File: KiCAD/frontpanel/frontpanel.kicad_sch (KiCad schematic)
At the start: 0 parts

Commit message: Drop empty stubs (PA/Driver/Balun/LPF_output/Front_Panel) from analog
None of these contributed components, nets, or PCB footprints on Rev A;
they were placeholder sub-sheets for future work. PA/Driver/Balun/
LPF_output will come back when the RF-chain board project is created
(a separate KiCAD/rf/ project, not part of analog). Front_Panel notes
were preserved by copying the text block into KiCAD/frontpanel/
frontpanel.kicad_sch first — the new frontpanel project is the actual
front-panel PCB.

Removed from analog.kicad_sch: five (sheet ...) blocks.
Removed from analog.kicad_pro: five UUID entries in the "sheets" list.
Deleted files: driver/pa/balun/lpf_output/front_panel.kicad_sch.

Rev A gerbers unaffected (fabricated 2026-07-14, byte-identical copy
preserved at KiCAD/analog/gerber/).

Co-Authored-By: Claude Opus 4.7 <noreply@anthropic.com>
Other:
- note added: "Front-panel vector board. Off-PCB. Connects to the main board's RJ45 J1 (on the Interface sheet) through a shielded CAT6 umbilical (T568B). See Documentation/front_panel_interface.md for wiring, grounding rules, and the open-items checklist. Parts to add here (all mark exclude_from_board = yes so KiCad does not try to route them on the main PCB): - Adafruit PCF8575 I2C 16-GPIO expander (I2C addr 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"
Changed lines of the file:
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@@
 	(generator_version "10.0")
 	(paper "A4")
+	(text "Front-panel vector board.\n\nOff-PCB. Connects to the main board's RJ45 J1 (on the Interface sheet)\nthrough a shielded CAT6 umbilical (T568B). See\nDocumentation/front_panel_interface.md for wiring, grounding rules,\nand the open-items checklist.\n\nParts to add here (all mark exclude_from_board = yes so KiCad\ndoes not try to route them on the main PCB):\n  - Adafruit PCF8575 I2C 16-GPIO expander (I2C addr 0x20)\n  - Winstar WH2004A 20x4 character LCD (driven in 4-bit mode by the PCF8575)\n  - 2x Bourns PEC11-4 mechanical encoders (STEP, FUNC)\n  - MBL-600 optical encoder (RS-422 differential, wired straight to the RJ45)\n  - Paddle jack (dit / dah -> PCF8575 GPIO)\n  - Front-panel LEDs (TX, fault, VFO-lock -> PCF8575 GPIO)\n  - Bypass caps at LCD Vcc and PCF8575 Vcc (10 uF + 100 nF each)\n  - LCD contrast trim pot, backlight series resistor"
+		(exclude_from_sim no)
+		(at 25.4 25.4 0)
+		(effects
+			(font
+				(size 1.27 1.27)
+			)
+			(justify left top)
+		)
+	)
 	(sheet_instances
 		(path "/"

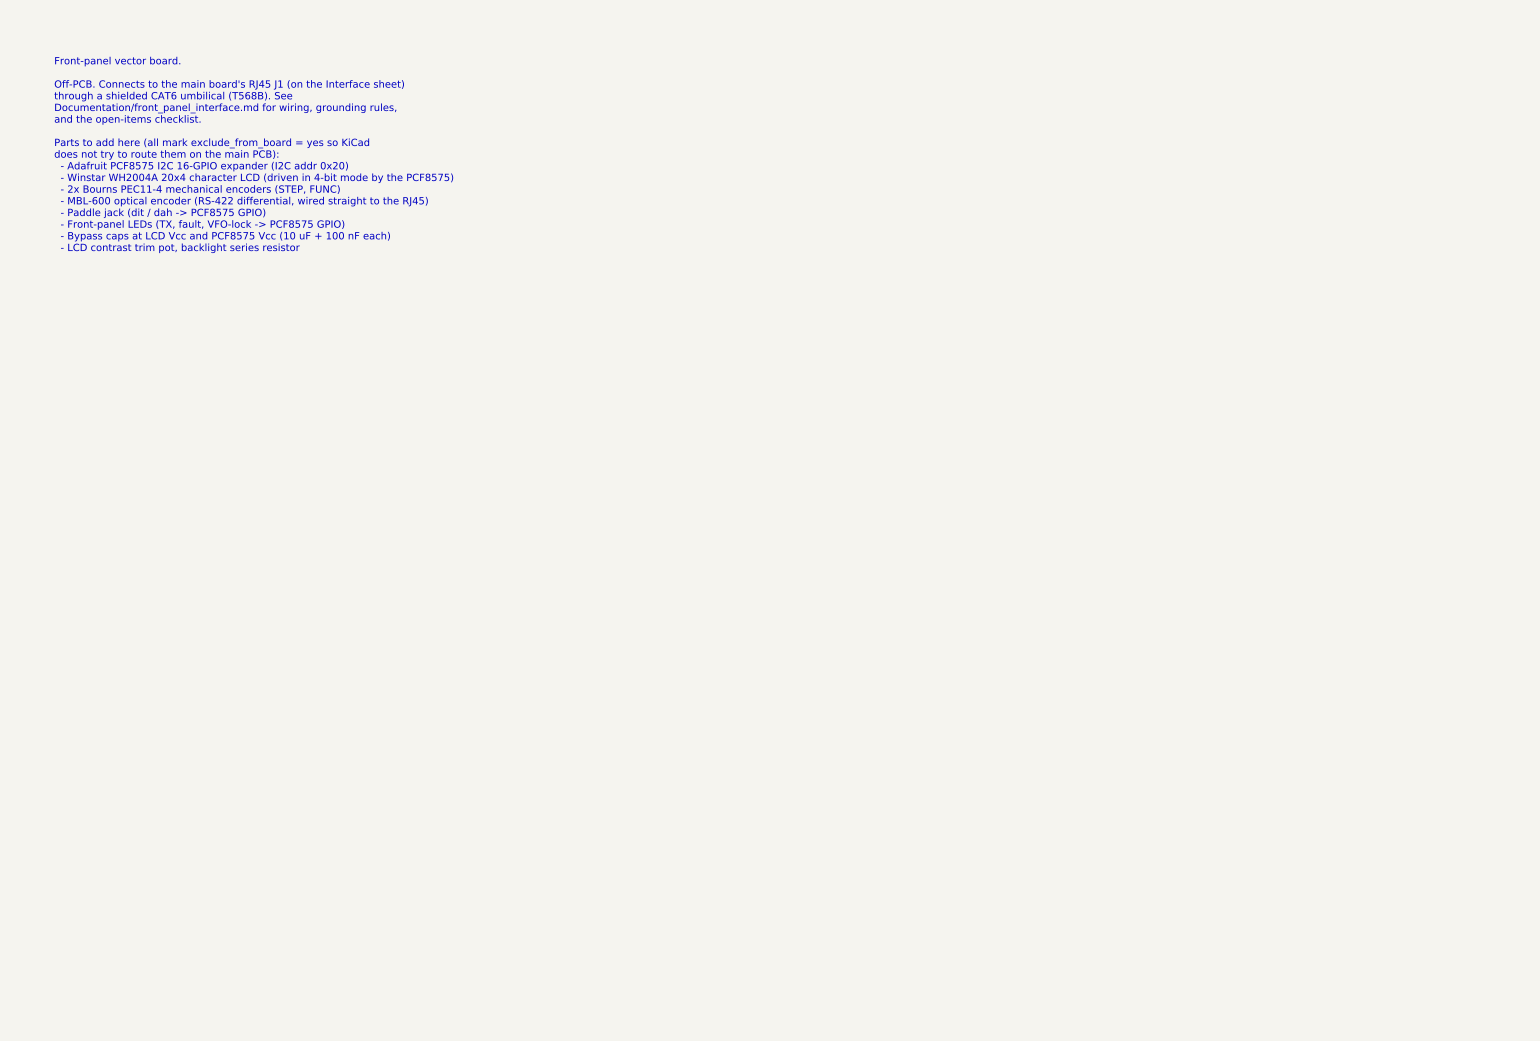
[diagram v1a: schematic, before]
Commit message: Front-panel PCB topology + I2C address plan alignment + 5734 symbol fix
Switch the front panel from a hand-wired vector board with a cut CAT6
pigtail to a real PCB with an Amphenol RJE1D-188-21401 socket at each
end of a commercial CAT6 patch cable. Shield ground stays single-point
at the analog board; the front-panel socket's shield-tab pads are left
floating on the schematic, with a GND-isolated PCB zone poured around
the connector body at layout time.

Reflect the current I2C address plan (updated 2026-07-15):
  - MCP4728  0x67  (was 0x62 in older docs -- reserves 0x62/0x63 for
                    future MCP4725 bias DACs)
  - STEP QT  0x37  (A0 jumper -- dodges the Metro's on-board MAX17048)
  - FUNC QT  0x38  (A1 jumper)
  - MAX17048 0x36  (documented as on the shared bus, not a private one)

Fix xmitter:Encoder_5734 (MBL600-100P-5L / Adafruit #5734) -- was a
3-pin single-ended stub, now the correct 6-pin RS-422 line-driver
symbol matching the actual datasheet (terminals 1=A, 2=B, 3=0V, 4=Vcc,
5=A-, 6=B-). Matches the AM26LS32 receiver on the analog interface sheet.

Add an optional second paddle path via the front-panel PCF8575 GPIO for
mechanical-build flexibility. Only one paddle path populated per build.

Reopen the RJE1D-188 footprint verification -- current footprint is
known wrong pending Rev A dry-fit; hold off on edits until Rev A arrives.

Sweeps stale post-reorg `KiCAD/interface.kicad_sch` paths to
`KiCAD/analog/interface.kicad_sch`.

Co-Authored-By: Claude Opus 4.7 <noreply@anthropic.com>
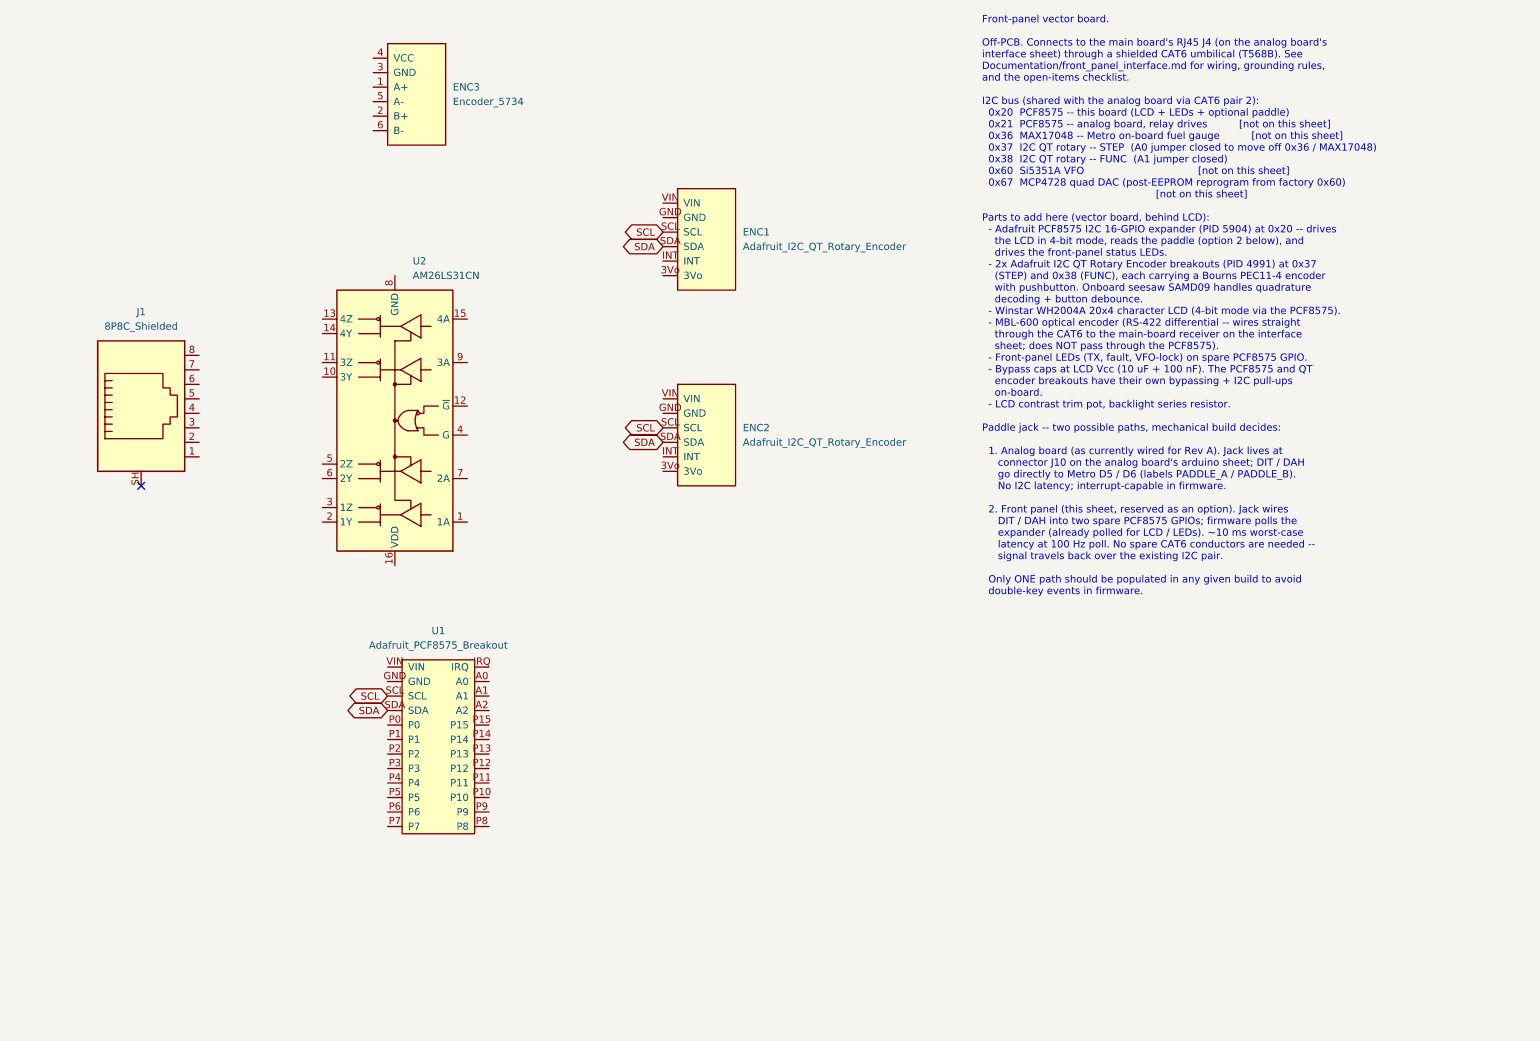
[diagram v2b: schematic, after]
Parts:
- added ENC1, ENC2: Adafruit_I2C_QT_Rotary_Encoder, xmitter:Adafruit_I2C_QT_Rotary_Encoder, symbol xmitter:Adafruit_I2C_QT_Rotary_Encoder
- added ENC3: Encoder_5734, Connector_PinHeader_2.54mm:PinHeader_1x06_P2.54mm_Vertical, symbol xmitter:Encoder_5734
- added J1: 8P8C_Shielded, xmitter:Amphenol_RJE1D-188_Horizontal_Shielded, symbol Connector:8P8C_Shielded
- added U1: Adafruit_PCF8575_Breakout, xmitter:Adafruit_PCF8575_Breakout, symbol xmitter:Adafruit_PCF8575_Breakout
- added U2: AM26LS31CN, Package_DIP:DIP-16_W7.62mm, symbol Interface:AM26LS31CN
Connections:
- new net SCL: ENC1.SCL, ENC2.SCL, U1.SCL
- new net SDA: ENC1.SDA, ENC2.SDA, U1.SDA
- no-connect marks 0 -> 1
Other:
- note added: "Front-panel vector board. Off-PCB. Connects to the main board's RJ45 J4 (on the analog board's interface sheet) through a shielded CAT6 umbilical (T568B). See Documentation/front_panel_interface.md for wiring, grounding rules, and the open-items checklist. I2C bus (shared with the analog board via CAT6 pair 2): 0x20 PCF8575 -- this board (LCD + LEDs + optional paddle) 0x21 PCF8575 -- analog board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"
- note removed: "Front-panel vector board. Off-PCB. Connects to the main board's RJ45 J1 (on the Interface sheet) through a shielded CAT6 umbilical (T568B). See Documentation/front_panel_interface.md for wiring, grounding rules, and the open-items checklist. Parts to add here (all mark exclude_from_board = yes so KiCad does not try to route them on the main PCB): - Adafruit PCF8575 I2C 16-GPIO expander (I2C addr 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"

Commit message: Front-panel schematic: complete wiring, MBL-600 pinout aligned with analog
Complete the front-panel schematic build-out. Initial MBL-600 <-> RJ45
wiring disagreed with the analog interface sheet's T568B pinout; rewired
to conform. ERC now passes with zero errors/warnings.

  - J1 (RJE1D-188): signal pins labeled per T568B, shield tabs NC
    (single-point ground stays at the analog board end).
  - ENC3 (MBL-600 / Adafruit #5734): A+/A-/B+/B- to RJ45 pins 3/6/7/8
    matching interface.kicad_sch J4.
  - LCD1 (WH2004A) 4-bit mode: DB4-DB7 to PCF8575 via LCD_D4..LCD_D7,
    DB0-DB3 marked NC, R/W tied to GND, RV1=10k contrast pot on V0.
  - Backlight: pin 15 to +5V direct; cathodes through R1/R2/R3
    (200/120/120R for lifetime-derated 15 mA per channel) into
    Q1/Q2/Q3 2N7000 low-side switches gated from PCF8575.

Add LCD_WH2004A symbol to xmitter.kicad_sym.

Also add datasheets for parts used: WH2004A LCD, Si5351-B (VFO),
AM26LS31 (MBL-600 line driver), scaa137 (Si5351 app note).

Co-Authored-By: Claude Opus 4.7 <noreply@anthropic.com>
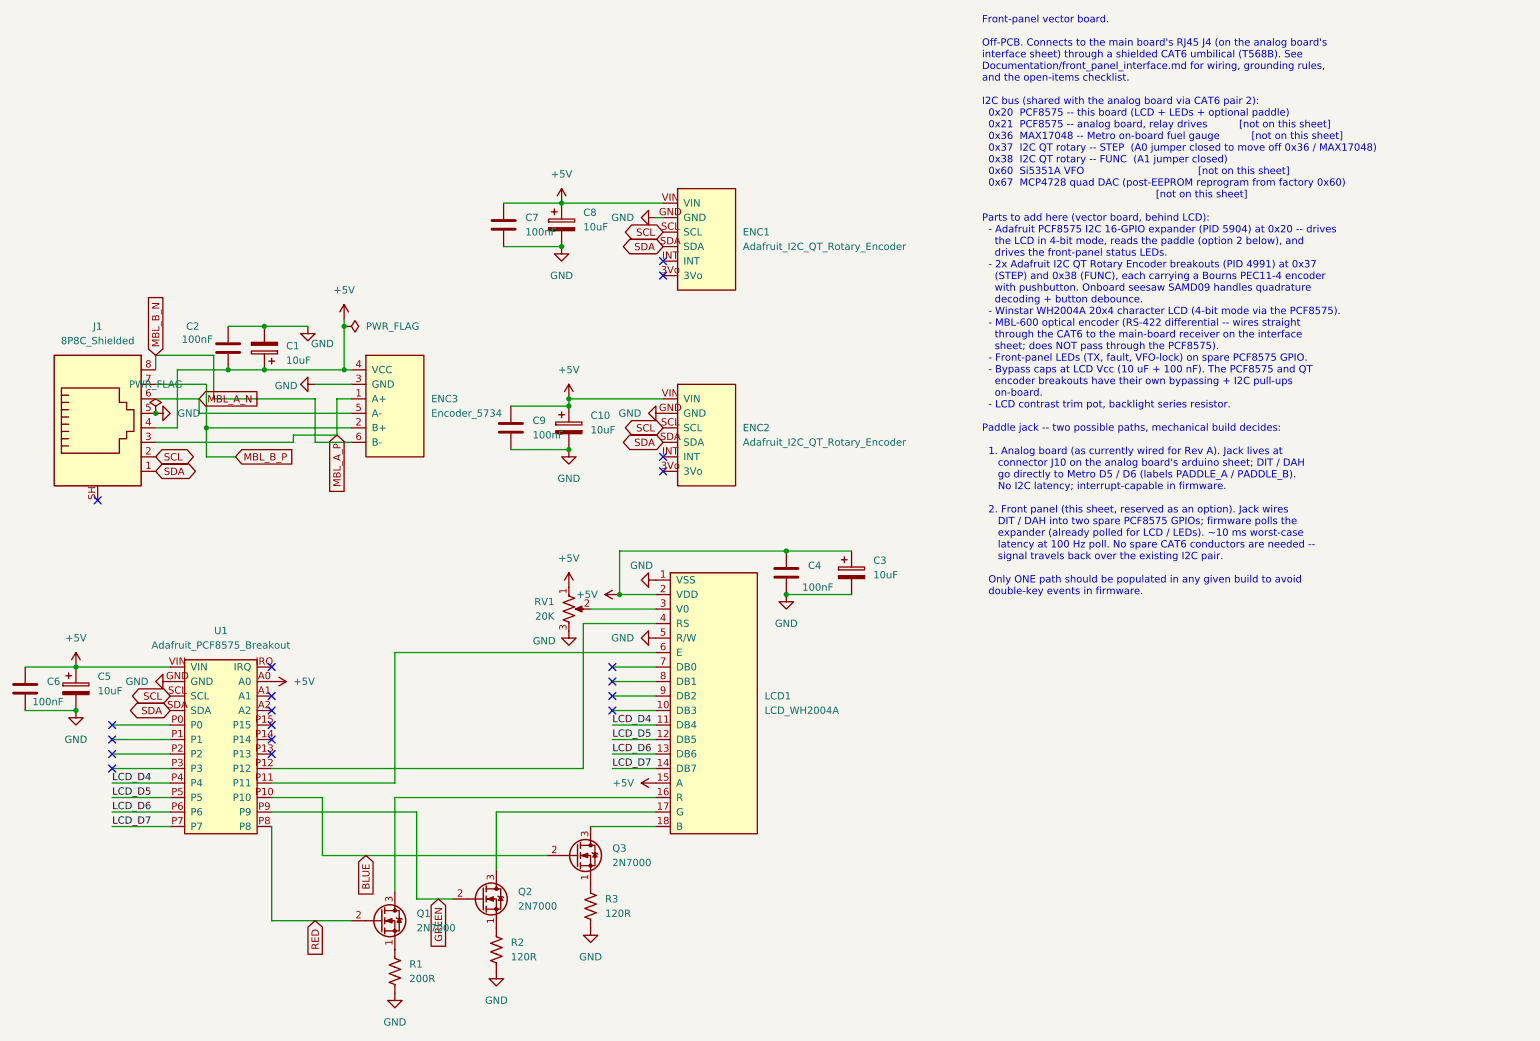
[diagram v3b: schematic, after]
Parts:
- removed U2: AM26LS31CN, Package_DIP:DIP-16_W7.62mm, symbol Interface:AM26LS31CN
- added C1, C10, C3, C5, C8: 10uF, symbol Device:C_Polarized
- added C2, C4, C6, C7, C9: 100nF, symbol Device:C
- added LCD1: LCD_WH2004A, Connector_PinHeader_2.54mm:PinHeader_1x18_P2.54mm_Vertical, symbol xmitter:LCD_WH2004A
- added Q1, Q2, Q3: 2N7000, Package_TO_SOT_THT:TO-92_Inline, symbol Transistor_FET:2N7000
- added R1: 200R, symbol Device:R_US
- added R2, R3: 120R, symbol Device:R_US
- added RV1: 20K, symbol Device:R_Potentiometer_US
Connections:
- net SCL: now also J1.2
- net SDA: now also J1.1
- net GND: now reaches ENC1.GND
- net GND: now also ENC2.GND, ENC3.3 (GND), J1.5, U1.GND, C1.2, C10.2, C2.1, C3.2, C4.2, C5.2, C6.2, C7.2, C8.2, C9.2, LCD1.1 (VSS), LCD1.5 (R/W), R1.2, R2.2, R3.2, RV1.3
- net +5V: now reaches ENC1.VIN
- net +5V: now also ENC2.VIN, ENC3.4 (VCC), J1.4, U1.A0, U1.VIN, C1.1, C10.1, C2.2, C3.1, C4.1, C5.1, C6.1, C7.1, C8.1, C9.1, LCD1.15 (A), LCD1.2 (VDD), RV1.1
- net BLUE: now reaches U1.P10
- net BLUE: now also Q3.2 (G)
- net at U1.P11: now also LCD1.6 (E)
- net at U1.P12: now also LCD1.4 (RS)
- net LCD_D4: now reaches U1.P4
- net LCD_D4: now also LCD1.11 (DB4)
- net LCD_D5: now reaches U1.P5
- net LCD_D5: now also LCD1.12 (DB5)
- net LCD_D6: now reaches U1.P6
- net LCD_D6: now also LCD1.13 (DB6)
- net LCD_D7: now reaches U1.P7
- net LCD_D7: now also LCD1.14 (DB7)
- net RED: now reaches U1.P8
- net RED: now also Q1.2 (G)
- net GREEN: now reaches U1.P9
- net GREEN: now also Q2.2 (G)
- net MBL_A_P: now reaches ENC3.1 (A+)
- net MBL_A_P: now also J1.3
- net MBL_B_P: now reaches ENC3.2 (B+)
- net MBL_B_P: now also J1.7
- net MBL_A_N: now reaches ENC3.5 (A-)
- net MBL_A_N: now also J1.6
- net MBL_B_N: now reaches ENC3.6 (B-)
- net MBL_B_N: now also J1.8
- new net: Q1.1 (S), R1.1
- new net: LCD1.16 (R), Q1.3 (D)
- new net: Q2.1 (S), R2.1
- new net: Q3.1 (S), R3.1
- new net: LCD1.17 (G), Q2.3 (D)
- new net: LCD1.18 (B), Q3.3 (D)
- new net: LCD1.3 (V0), RV1.2
- no-connect marks 1 -> 19
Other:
- moved on the sheet: ENC3, J1, U1
